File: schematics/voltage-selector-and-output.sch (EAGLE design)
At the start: 28 parts, among them IC1 5V, IC2 MIC2941, IC3 MCP41010P, IC5 12V, IC6 ATTINY85

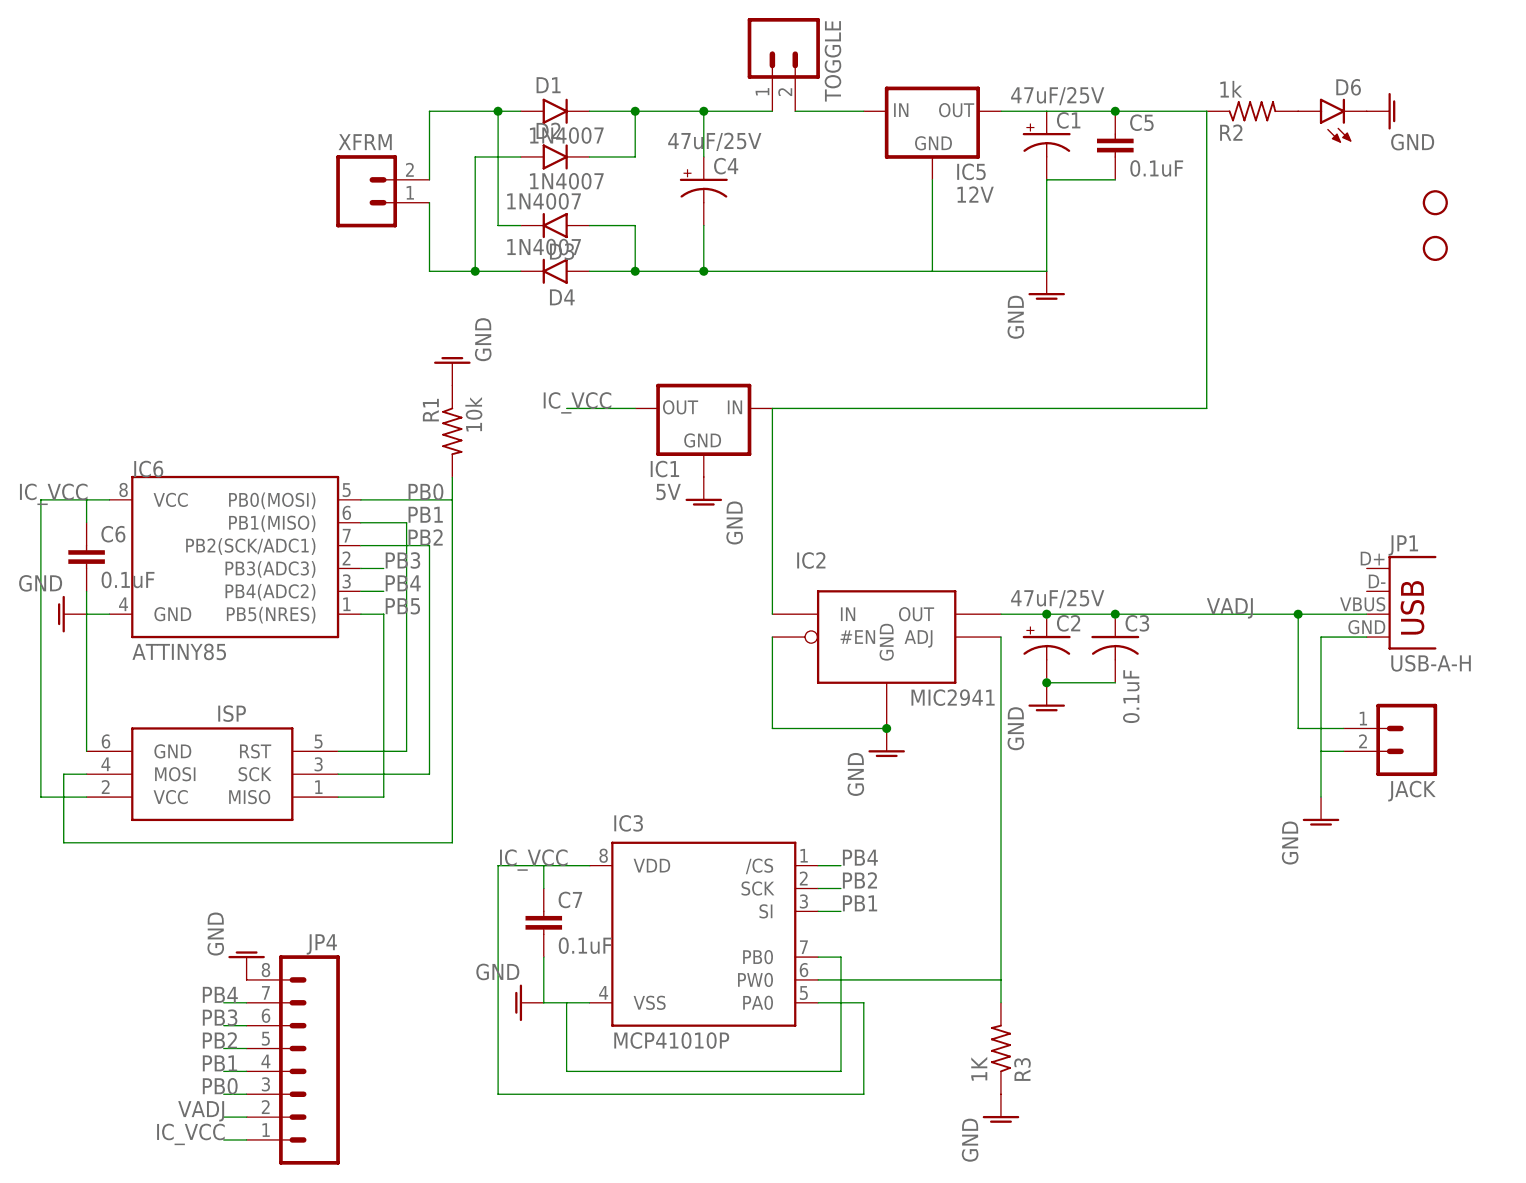
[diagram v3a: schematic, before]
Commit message: Optimizing the location of the components on the board and fixing the schematic
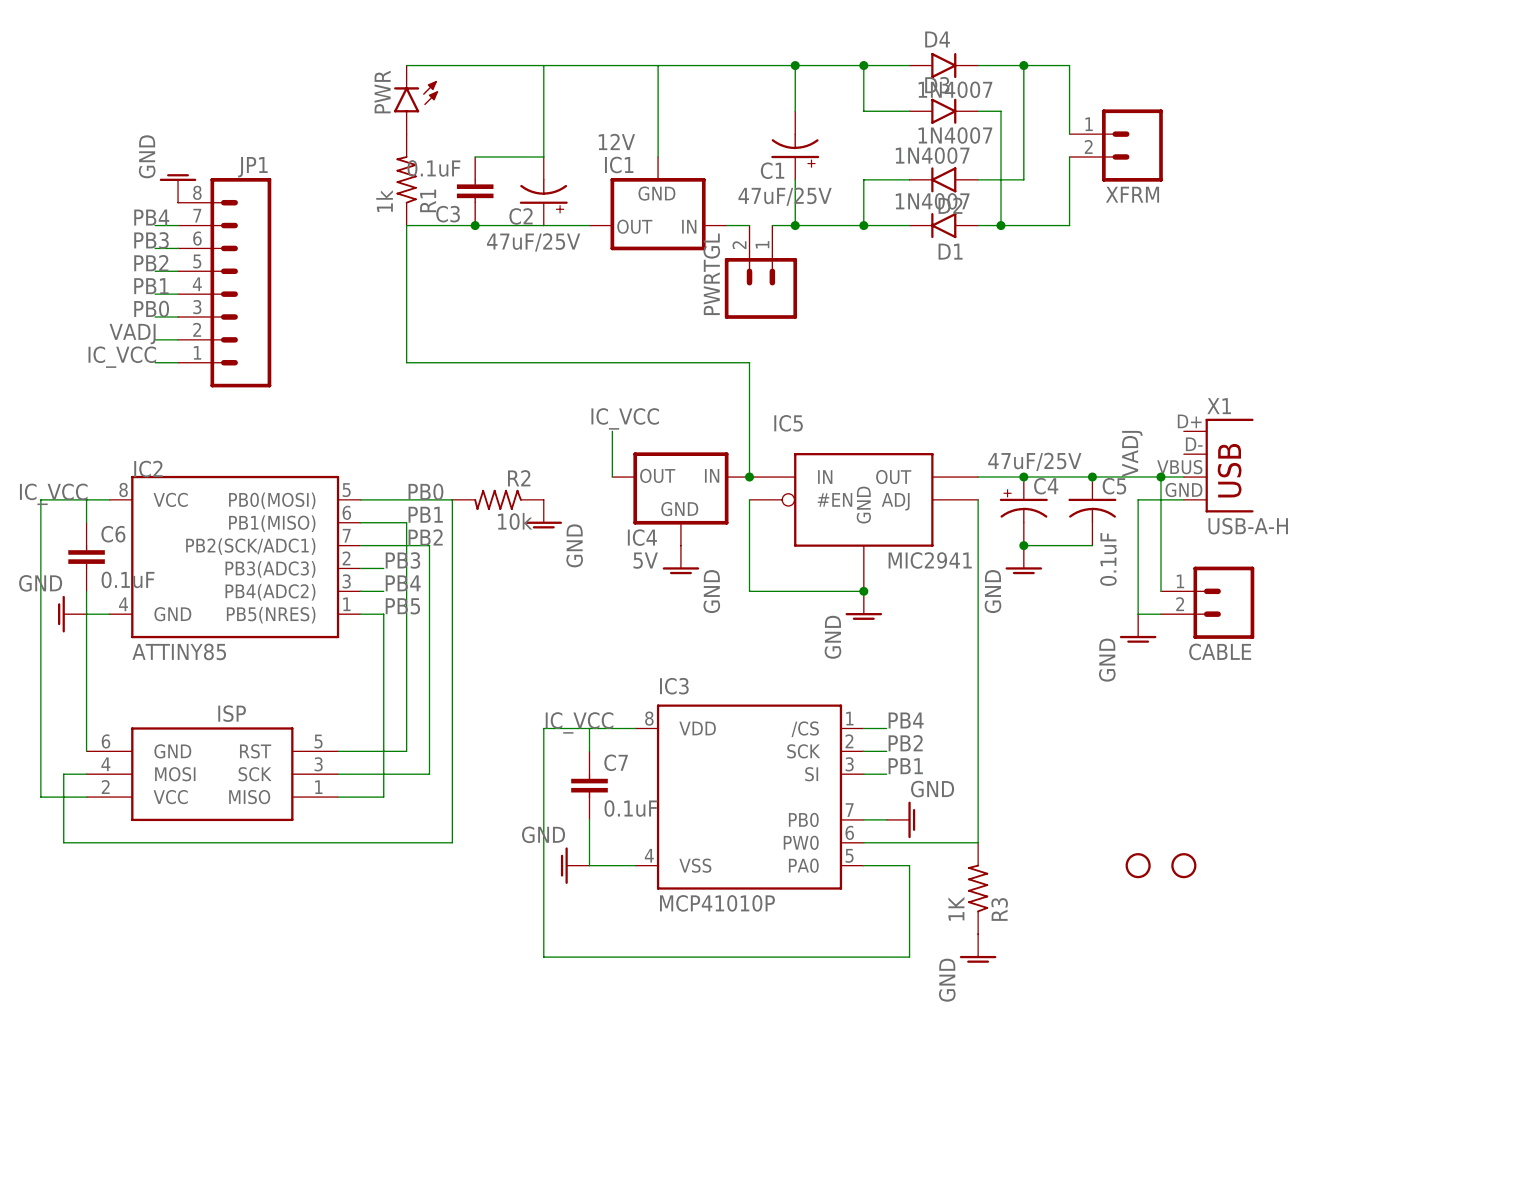
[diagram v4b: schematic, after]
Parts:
- removed D6: (no value), SparkFun-LED:LED-3MM-NO_SILK
- removed IC6: ATTINY85, SparkFun:ATTINY13DIP
- removed JACK, TOGGLE: (no value), SparkFun:M02PTH
- removed JP4: (no value), SparkFun:M081X08
- added CABLE, PWRTGL: (no value), SparkFun:M02PTH
- added IC4: 5V, v-reg:78XXS
- added PWR: (no value), SparkFun-LED:LED-3MM-NO_SILK
- added X1: USB-A-H, SparkFun-Connectors:USB-A-H
- C3: device minimidi:C-US025-025X050 -> SparkFun-Capacitors:CAPPTH
- C5: device SparkFun-Capacitors:CAPPTH -> minimidi:C-US025-025X050
- IC1: value 5V -> 12V
- IC2: value MIC2941 -> ATTINY85; device bbsup:MIC2941 -> SparkFun:ATTINY13DIP
- IC5: value 12V -> MIC2941; device v-reg:78XXS -> bbsup:MIC2941
- JP1: value USB-A-H -> (none); device SparkFun-Connectors:USB-A-H -> SparkFun:M081X08
- R1: value 10k -> 1k
- R2: value 1k -> 10k
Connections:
- removed net N$11: JACK.1
- removed net N$3: D2.A, D4.C, XFRM.1
- new net N$5: C1.-, C2.-, C3.2, D3.A, D4.A, IC1.GND, PWR.C
- net AGND: now also CABLE.2, D2.A, D4.C, IC4.GND, IC5.#EN, JP1.8, R2.1, X1.GND, XFRM.1; no longer C1.-, C2.-, C3.2, D3.A, D4.A, D6.C, IC1.GND, IC2.#EN, IC6.GND, JACK.2, JP1.GND, JP4.8, R1.1
- net IC_VCC: now also IC2.VCC, IC4.OUT, JP1.1; no longer IC1.OUT, IC6.VCC, JP4.1
- net N$1: now also IC1.IN, PWRTGL.2; no longer IC5.IN, TOGGLE.2
- net N$10: now also PWR.A, R1.2; no longer D6.A, R2.2
- net N$4: now also IC5.ADJ; no longer IC2.ADJ
- net N$9: now also C1.+, PWRTGL.1; no longer C4.+, TOGGLE.1
- net PB0: now also IC2.PB0(MOSI), JP1.3, R2.2; no longer IC6.PB0(MOSI), JP4.3, R1.2
- net PB1: now also IC2.PB1(MISO), JP1.4; no longer IC6.PB1(MISO), JP4.4
- net PB2: now also IC2.PB2(SCK/ADC1), JP1.5; no longer IC6.PB2(SCK/ADC1), JP4.5
- net PB3: now also IC2.PB3(ADC3), JP1.6; no longer IC6.PB3(ADC3), JP4.6
- net PB4: now also IC2.PB4(ADC2), JP1.7; no longer IC6.PB4(ADC2), JP4.7
- net PB5: now also IC2.PB5(NRES); no longer IC6.PB5(NRES)
- net RECTIFIED_12VCC: now also C2.+, C3.1, IC1.OUT, IC4.IN, IC5.IN, R1.1; no longer C1.+, C5.1, IC1.IN, IC2.IN, IC5.OUT, R2.1
- net VADJ: now also C4.+, C5.1, CABLE.1, IC5.OUT, JP1.2, X1.VBUS; no longer C2.+, C3.1, IC2.OUT, JP1.VBUS, JP4.2
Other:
- moved on the sheet: C1, C2, C3, C4, C5, C7, D1, D2, D3, D4, IC1, IC3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

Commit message: The 12v regulator was kinda too much, now that I think about it
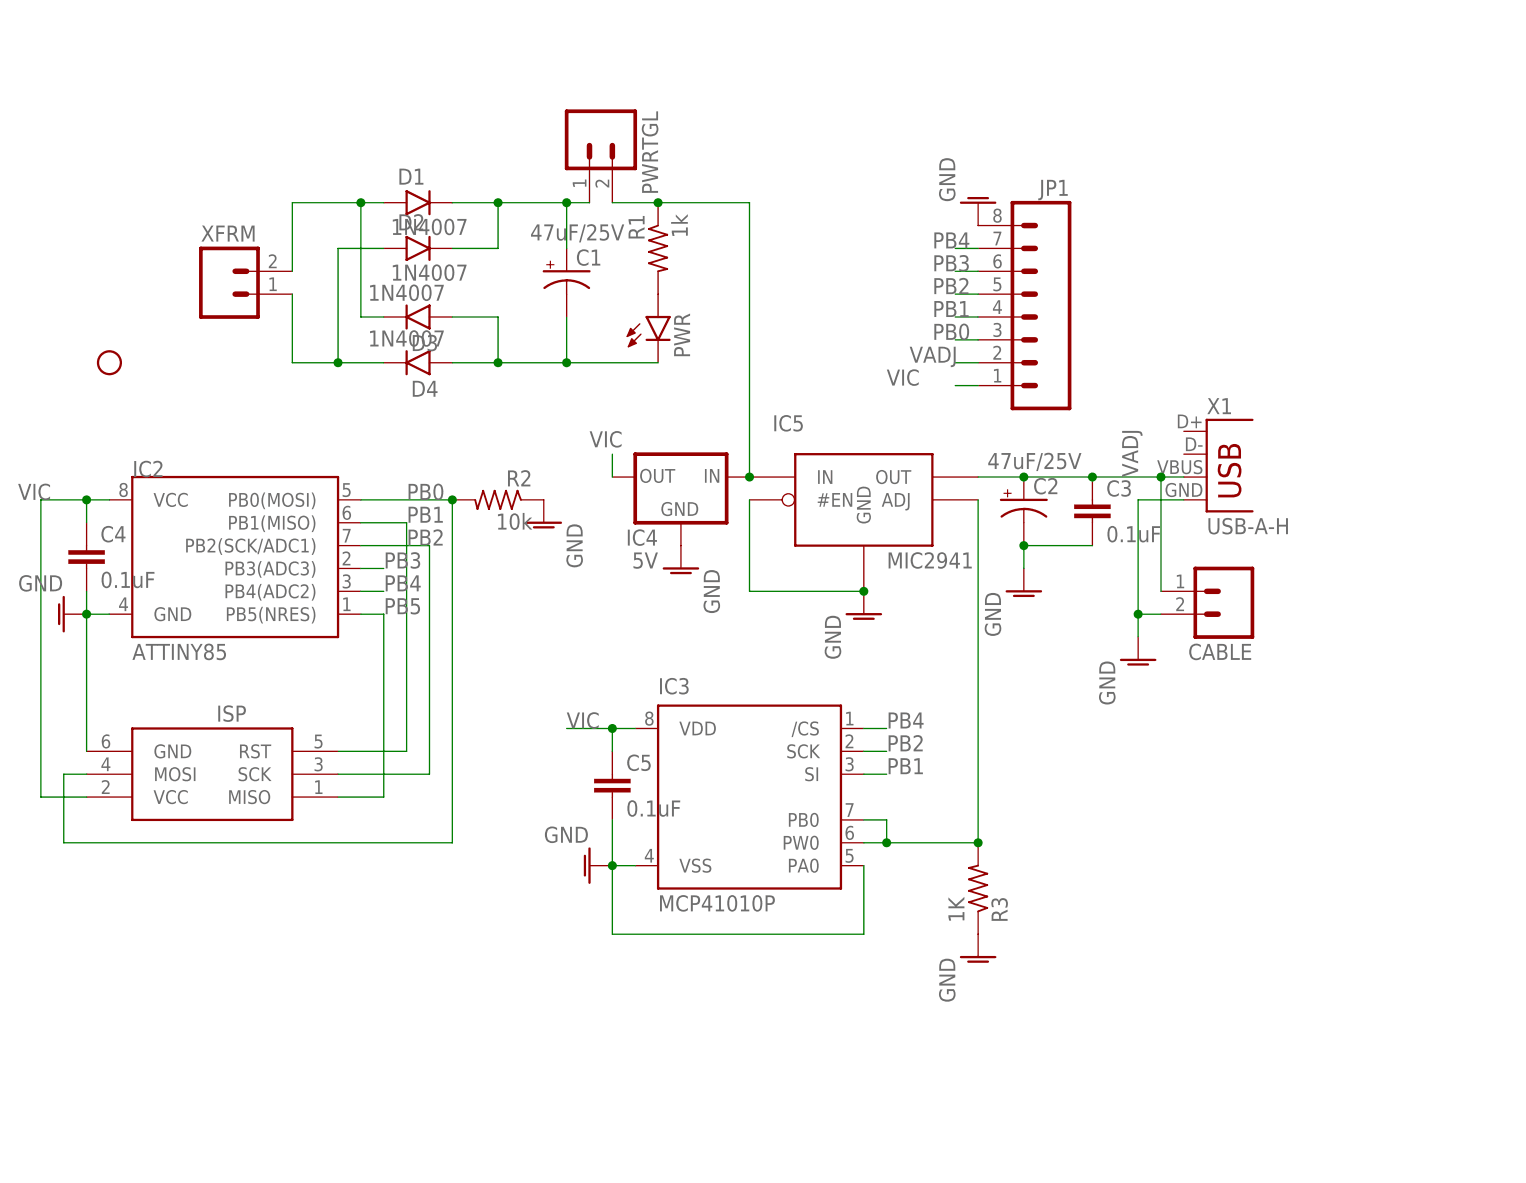
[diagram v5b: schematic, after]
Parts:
- removed C6, C7: 0.1uF, SparkFun-Capacitors:CAPPTH
- removed IC1: 12V, v-reg:78XXS
- removed STANDOFF2: STAND-OFF, SparkFun-Electromechanical:STAND-OFF
- C4: value 47uF/25V -> 0.1uF; device minimidi:CPOL-USE2.5-6 -> SparkFun-Capacitors:CAPPTH
- C5: device minimidi:C-US025-025X050 -> SparkFun-Capacitors:CAPPTH
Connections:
- removed net IC_VCC: C6.1, C7.1, IC2.VCC, IC3.PA0, IC3.VDD, IC4.OUT, ISP.VCC, JP1.1
- removed net N$1: IC1.IN, PWRTGL.2
- removed net RECTIFIED_12VCC: C2.+, C3.1, IC1.OUT, IC4.IN, IC5.IN, R1.1
- new net GND: D2.A, D4.C, XFRM.1
- new net VCC: IC4.IN, IC5.IN, PWRTGL.2, R1.1
- new net VIC: C4.1, C5.1, IC2.VCC, IC3.VDD, IC4.OUT, ISP.VCC, JP1.1
- net AGND: now also C2.-, C3.2, C4.2, IC3.PA0; no longer C4.-, C6.2, C7.2, D2.A, D4.C, IC3.PB0, XFRM.1
- net N$4: now also IC3.PB0
- net N$5: no longer C2.-, C3.2, IC1.GND
- net VADJ: now also C2.+, C3.1; no longer C4.+, C5.1
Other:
- moved on the sheet: C1, C2, C3, C5, D1, D2, D3, D4, JP1, PWR, PWRTGL, R1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

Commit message: Tweak tweak
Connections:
- new net N$1: IC3.PB0
- new net N$3: IC3.PA0
- net AGND: no longer IC3.PA0
- net N$4: no longer IC3.PB0
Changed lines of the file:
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@@
 <instance part="ISP" gate="G$1" x="-22.86" y="154.94" rot="R180"/>
 <instance part="GND3" gate="VR1" x="-40.64" y="172.72" rot="R270"/>
-<instance part="GND6" gate="VR1" x="17.78" y="144.78" rot="R270"/>
+<instance part="GND6" gate="VR1" x="15.24" y="144.78" rot="R270"/>
 <instance part="D1" gate="1" x="0" y="218.44"/>
 <instance part="D2" gate="1" x="0" y="213.36"/>
@@
 <pinref part="JP1" gate="G$1" pin="1"/>
 <wire x1="60.96" y1="198.12" x2="58.42" y2="198.12" width="0.1524" layer="91"/>
-<label x="50.8" y="198.12" size="1.778" layer="95"/>
+<label x="55.88" y="198.12" size="1.778" layer="95"/>
 </segment>
 <segment>
@@
 <pinref part="R3" gate="G$1" pin="2"/>
 <pinref part="IC5" gate="G$1" pin="ADJ"/>
-<wire x1="48.26" y1="147.32" x2="50.8" y2="147.32" width="0.1524" layer="91"/>
 <junction x="60.96" y="147.32"/>
-<junction x="50.8" y="147.32"/>
-<wire x1="50.8" y1="147.32" x2="60.96" y2="147.32" width="0.1524" layer="91"/>
-<pinref part="IC3" gate="P1" pin="PB0"/>
-<wire x1="48.26" y1="149.86" x2="50.8" y2="149.86" width="0.1524" layer="91"/>
-<wire x1="50.8" y1="149.86" x2="50.8" y2="147.32" width="0.1524" layer="91"/>
+<wire x1="48.26" y1="147.32" x2="60.96" y2="147.32" width="0.1524" layer="91"/>
 </segment>
 </net>
@@
 <net name="AGND" class="0">
 <segment>
-<pinref part="IC3" gate="P1" pin="VSS"/>
-<pinref part="GND6" gate="VR1" pin="AGND"/>
-<wire x1="22.86" y1="144.78" x2="20.32" y2="144.78" width="0.1524" layer="91"/>
-<pinref part="C5" gate="G$1" pin="2"/>
-<wire x1="20.32" y1="149.86" x2="20.32" y2="144.78" width="0.1524" layer="91"/>
-<junction x="20.32" y="144.78"/>
-<pinref part="IC3" gate="P1" pin="PA0"/>
-<wire x1="48.26" y1="144.78" x2="48.26" y2="137.16" width="0.1524" layer="91"/>
-<wire x1="48.26" y1="137.16" x2="20.32" y2="137.16" width="0.1524" layer="91"/>
-<wire x1="20.32" y1="137.16" x2="20.32" y2="144.78" width="0.1524" layer="91"/>
-</segment>
-<segment>
 <pinref part="IC2" gate="G$1" pin="GND"/>
 <pinref part="GND3" gate="VR1" pin="AGND"/>
@@
 <pinref part="JP1" gate="G$1" pin="8"/>
 </segment>
-</net>
+<segment>
+<pinref part="IC3" gate="P1" pin="VSS"/>
+<pinref part="GND6" gate="VR1" pin="AGND"/>
+<wire x1="22.86" y1="144.78" x2="20.32" y2="144.78" width="0.1524" layer="91"/>
+<pinref part="C5" gate="G$1" pin="2"/>
+<wire x1="20.32" y1="144.78" x2="17.78" y2="144.78" width="0.1524" layer="91"/>
+<wire x1="20.32" y1="149.86" x2="20.32" y2="144.78" width="0.1524" layer="91"/>
+<junction x="20.32" y="144.78"/>
+</segment>
+</net>
+<net name="N$1" class="0">
+<segment>
+<pinref part="IC3" gate="P1" pin="PB0"/>
+<wire x1="48.26" y1="149.86" x2="53.34" y2="149.86" width="0.1524" layer="91"/>
+</segment>
+</net>
+<net name="N$3" class="0">
+<segment>
+<pinref part="IC3" gate="P1" pin="PA0"/>
+<wire x1="48.26" y1="144.78" x2="48.26" y2="137.16" width="0.1524" layer="91"/>
+<wire x1="48.26" y1="137.16" x2="20.32" y2="137.16" width="0.1524" layer="91"/>
+</segment>
+</net>

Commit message: Figured out the error in my drawing, finally
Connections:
- removed net N$3: IC3.PA0
- removed net N$4: IC3.PW0, IC5.ADJ, R3.2
- net AGND: now also IC3.PA0
- net N$1: now also IC3.PW0, IC5.ADJ, R3.2
- net PB4: no longer JP1.7
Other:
- moved on the sheet: JP1
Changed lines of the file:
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@@
 <instance part="GND5" gate="VR1" x="27.94" y="177.8" rot="MR0"/>
 <instance part="GND8" gate="VR1" x="12.7" y="182.88" rot="MR0"/>
-<instance part="JP1" gate="G$1" x="66.04" y="205.74" rot="MR0"/>
-<instance part="GND7" gate="VR1" x="60.96" y="218.44" rot="MR180"/>
+<instance part="JP1" gate="G$1" x="63.5" y="213.36" rot="R180"/>
+<instance part="GND7" gate="VR1" x="58.42" y="200.66"/>
 <instance part="IC4" gate="1" x="27.94" y="187.96" rot="MR0"/>
 <instance part="R2" gate="G$1" x="7.62" y="185.42" rot="MR0"/>
@@
 <segment>
 <pinref part="JP1" gate="G$1" pin="1"/>
-<wire x1="60.96" y1="198.12" x2="58.42" y2="198.12" width="0.1524" layer="91"/>
-<label x="55.88" y="198.12" size="1.778" layer="95"/>
+<wire x1="58.42" y1="220.98" x2="55.88" y2="220.98" width="0.1524" layer="91"/>
+<label x="55.88" y="220.98" size="1.778" layer="95" rot="MR0"/>
 </segment>
 <segment>
@@
 <segment>
 <pinref part="JP1" gate="G$1" pin="2"/>
-<wire x1="60.96" y1="200.66" x2="58.42" y2="200.66" width="0.1524" layer="91"/>
-<label x="53.34" y="200.66" size="1.778" layer="95"/>
+<wire x1="58.42" y1="218.44" x2="55.88" y2="218.44" width="0.1524" layer="91"/>
+<label x="55.88" y="218.44" size="1.778" layer="95" rot="MR0"/>
 </segment>
 </net>
@@
 <segment>
 <pinref part="JP1" gate="G$1" pin="5"/>
-<wire x1="60.96" y1="208.28" x2="58.42" y2="208.28" width="0.1524" layer="91"/>
-<label x="55.88" y="208.28" size="1.778" layer="95"/>
+<wire x1="58.42" y1="210.82" x2="55.88" y2="210.82" width="0.1524" layer="91"/>
+<label x="55.88" y="210.82" size="1.778" layer="95" rot="MR0"/>
 </segment>
 </net>
@@
 <segment>
 <pinref part="JP1" gate="G$1" pin="4"/>
-<wire x1="60.96" y1="205.74" x2="58.42" y2="205.74" width="0.1524" layer="91"/>
-<label x="55.88" y="205.74" size="1.778" layer="95"/>
+<wire x1="58.42" y1="213.36" x2="55.88" y2="213.36" width="0.1524" layer="91"/>
+<label x="55.88" y="213.36" size="1.778" layer="95" rot="MR0"/>
 </segment>
 <segment>
@@
 <segment>
 <pinref part="JP1" gate="G$1" pin="6"/>
-<wire x1="60.96" y1="210.82" x2="58.42" y2="210.82" width="0.1524" layer="91"/>
-<label x="55.88" y="210.82" size="1.778" layer="95"/>
+<wire x1="58.42" y1="208.28" x2="55.88" y2="208.28" width="0.1524" layer="91"/>
+<label x="55.88" y="208.28" size="1.778" layer="95" rot="MR0"/>
 </segment>
 </net>
@@
 <wire x1="-7.62" y1="175.26" x2="-5.08" y2="175.26" width="0.1524" layer="91"/>
 <label x="-5.08" y="175.26" size="1.778" layer="95"/>
-</segment>
-<segment>
-<pinref part="JP1" gate="G$1" pin="7"/>
-<wire x1="60.96" y1="213.36" x2="58.42" y2="213.36" width="0.1524" layer="91"/>
-<label x="55.88" y="213.36" size="1.778" layer="95"/>
 </segment>
 <segment>
@@
 <segment>
 <pinref part="JP1" gate="G$1" pin="3"/>
-<wire x1="60.96" y1="203.2" x2="58.42" y2="203.2" width="0.1524" layer="91"/>
-<label x="55.88" y="203.2" size="1.778" layer="95"/>
-</segment>
-</net>
-<net name="N$4" class="0">
-<segment>
-<pinref part="IC3" gate="P1" pin="PW0"/>
-<wire x1="60.96" y1="185.42" x2="60.96" y2="147.32" width="0.1524" layer="91"/>
-<pinref part="R3" gate="G$1" pin="2"/>
-<pinref part="IC5" gate="G$1" pin="ADJ"/>
-<junction x="60.96" y="147.32"/>
-<wire x1="48.26" y1="147.32" x2="60.96" y2="147.32" width="0.1524" layer="91"/>
+<wire x1="58.42" y1="215.9" x2="55.88" y2="215.9" width="0.1524" layer="91"/>
+<label x="55.88" y="215.9" size="1.778" layer="95" rot="MR0"/>
 </segment>
 </net>
@@
 <wire x1="20.32" y1="149.86" x2="20.32" y2="144.78" width="0.1524" layer="91"/>
 <junction x="20.32" y="144.78"/>
-</segment>
-</net>
-<net name="N$1" class="0">
-<segment>
-<pinref part="IC3" gate="P1" pin="PB0"/>
-<wire x1="48.26" y1="149.86" x2="53.34" y2="149.86" width="0.1524" layer="91"/>
-</segment>
-</net>
-<net name="N$3" class="0">
-<segment>
 <pinref part="IC3" gate="P1" pin="PA0"/>
 <wire x1="48.26" y1="144.78" x2="48.26" y2="137.16" width="0.1524" layer="91"/>
 <wire x1="48.26" y1="137.16" x2="20.32" y2="137.16" width="0.1524" layer="91"/>
-</segment>
-</net>
+<wire x1="20.32" y1="144.78" x2="20.32" y2="137.16" width="0.1524" layer="91"/>
+</segment>
+</net>
+<net name="N$1" class="0">
+<segment>
+<pinref part="IC3" gate="P1" pin="PB0"/>
+<wire x1="48.26" y1="149.86" x2="53.34" y2="149.86" width="0.1524" layer="91"/>
+<pinref part="IC3" gate="P1" pin="PW0"/>
+<wire x1="60.96" y1="185.42" x2="60.96" y2="147.32" width="0.1524" layer="91"/>
+<pinref part="R3" gate="G$1" pin="2"/>
+<pinref part="IC5" gate="G$1" pin="ADJ"/>
+<junction x="60.96" y="147.32"/>
+<wire x1="48.26" y1="147.32" x2="53.34" y2="147.32" width="0.1524" layer="91"/>
+<wire x1="53.34" y1="147.32" x2="60.96" y2="147.32" width="0.1524" layer="91"/>
+<wire x1="53.34" y1="149.86" x2="53.34" y2="147.32" width="0.1524" layer="91"/>
+<junction x="53.34" y="147.32"/>
+</segment>
+</net>
